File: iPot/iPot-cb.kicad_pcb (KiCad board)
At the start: 2 copper layers, 100 x 100 mm, 66 parts, among them CON1 12VDC, IC1 ATMEGA644-P, IC2 L298, P1 MOT2, P10 I2C3, P11 I2C4, P12 UART, P13 USB_PWR2, P14 ANALOG_IN, P15 PWM_IO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

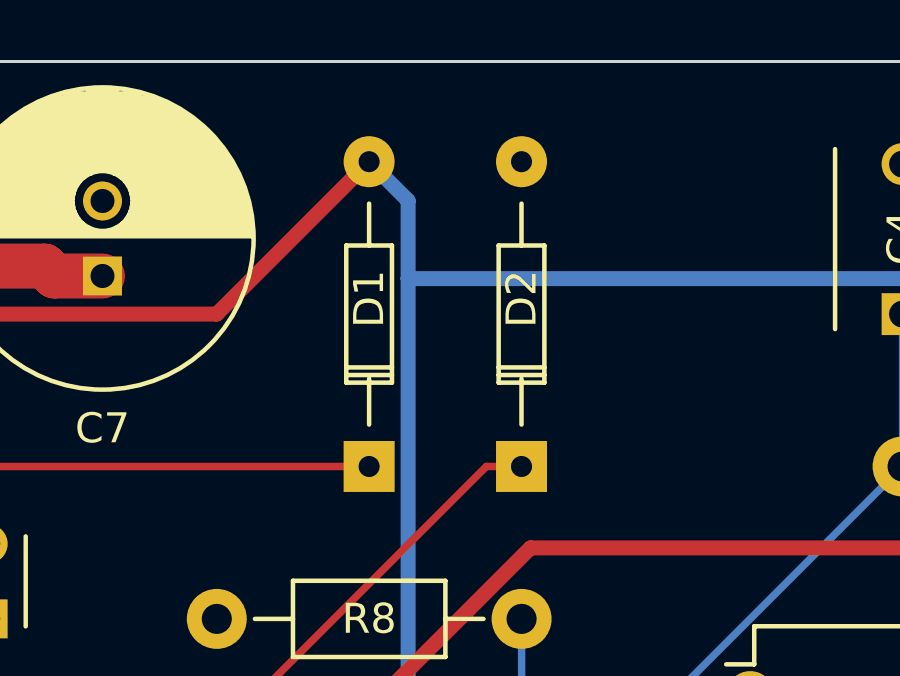
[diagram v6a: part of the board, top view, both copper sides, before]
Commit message: Fix diode footprint
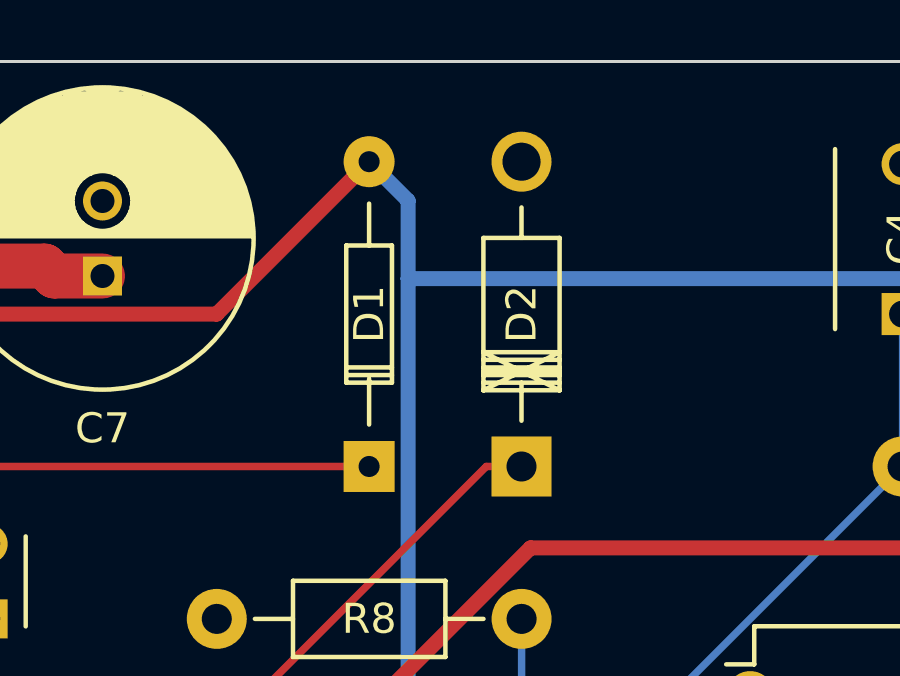
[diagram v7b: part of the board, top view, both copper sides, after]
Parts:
- D2: footprint Diodes_ThroughHole:Diode_DO-35_SOD27_Horizontal_RM10 -> Diodes_ThroughHole:Diode_DO-41_SOD81_Horizontal_RM10
- R7: value 270 -> 390
- R8: value 1k -> 680
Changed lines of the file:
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@@
     (links 170)
     (no_connects 1)
-    (area 49.511474 49.949999 152.490046 150.380714)
+    (area 49.949999 49.949999 150.050001 150.050001)
     (thickness 1.6)
     (drawings 5)
@@
     (descr "Diode, DO-35,  SOD27, Horizontal, RM 10mm")
     (tags "Diode, DO-35, SOD27, Horizontal, RM 10mm, 1N4148,")
-    (fp_text reference D1 (at 5.588 0 90) (layer F.SilkS)
+    (fp_text reference D1 (at 5.08 0 90) (layer F.SilkS)
       (effects (font (size 1 1) (thickness 0.15)))
     )
@@
     (pad 1 thru_hole rect (at 0.00052 -0.00254 270) (size 1.69926 1.69926) (drill 0.70104) (layers *.Cu *.Mask F.SilkS)
       (net 3 "Net-(C2-Pad1)"))
-    (model Diodes_ThroughHole.3dshapes/Diode_DO-35_SOD27_Horizontal_RM10.wrl
-      (at (xyz 0.2 0 0))
-      (scale (xyz 0.4 0.4 0.4))
-      (rotate (xyz 0 0 180))
-    )
-  )
-  (module Diodes_ThroughHole:Diode_DO-35_SOD27_Horizontal_RM10 locked (layer F.Cu)
-    (at 109.22 63.5 90)
-    (descr "Diode, DO-35,  SOD27, Horizontal, RM 10mm")
-    (tags "Diode, DO-35, SOD27, Horizontal, RM 10mm, 1N4148,")
-    (fp_text reference D2 (at 5.588 0 90) (layer F.SilkS)
-      (effects (font (size 1 1) (thickness 0.15)))
-    )
-    (fp_text value 1N5818 (at 4.41452 -3.55854 90) (layer F.Fab)
-      (effects (font (size 1 1) (thickness 0.15)))
-    )
-    (fp_line (start 7.36652 -0.00254) (end 8.76352 -0.00254) (layer F.SilkS) (width 0.15))
-    (fp_line (start 2.92152 -0.00254) (end 1.39752 -0.00254) (layer F.SilkS) (width 0.15))
-    (fp_line (start 3.30252 -0.76454) (end 3.30252 0.75946) (layer F.SilkS) (width 0.15))
-    (fp_line (start 3.04852 -0.76454) (end 3.04852 0.75946) (layer F.SilkS) (width 0.15))
-    (fp_line (start 2.79452 -0.00254) (end 2.79452 0.75946) (layer F.SilkS) (width 0.15))
-    (fp_line (start 2.79452 0.75946) (end 7.36652 0.75946) (layer F.SilkS) (width 0.15))
-    (fp_line (start 7.36652 0.75946) (end 7.36652 -0.76454) (layer F.SilkS) (width 0.15))
-    (fp_line (start 7.36652 -0.76454) (end 2.79452 -0.76454) (layer F.SilkS) (width 0.15))
-    (fp_line (start 2.79452 -0.76454) (end 2.79452 -0.00254) (layer F.SilkS) (width 0.15))
-    (pad 2 thru_hole circle (at 10.16052 -0.00254 270) (size 1.69926 1.69926) (drill 0.70104) (layers *.Cu *.Mask F.SilkS)
-      (net 2 GND))
-    (pad 1 thru_hole rect (at 0.00052 -0.00254 270) (size 1.69926 1.69926) (drill 0.70104) (layers *.Cu *.Mask F.SilkS)
-      (net 4 "Net-(C2-Pad2)"))
     (model Diodes_ThroughHole.3dshapes/Diode_DO-35_SOD27_Horizontal_RM10.wrl
       (at (xyz 0.2 0 0))
@@
       (effects (font (size 1 1) (thickness 0.15)))
     )
-    (fp_text value 270 (at 5.08 3.81) (layer F.Fab)
+    (fp_text value 390 (at 5.08 3.81) (layer F.Fab)
       (effects (font (size 1 1) (thickness 0.15)))
     )
@@
       (effects (font (size 1 1) (thickness 0.15)))
     )
-    (fp_text value 1k (at 5.08 3.81 180) (layer F.Fab)
+    (fp_text value 680 (at 5.08 3.81 180) (layer F.Fab)
       (effects (font (size 1 1) (thickness 0.15)))
     )
@@
     (pad 1 thru_hole circle (at -8.75 -3 90) (size 4 4) (drill 2.5) (layers *.Cu *.Mask F.SilkS))
   )
+  (module Diodes_ThroughHole:Diode_DO-41_SOD81_Horizontal_RM10 (layer F.Cu)
+    (at 109.22 63.5 90)
+    (descr "Diode, DO-41, SOD81, Horizontal, RM 10mm,")
+    (tags "Diode, DO-41, SOD81, Horizontal, RM 10mm, 1N4007, SB140,")
+    (fp_text reference D2 (at 5.08 0 90) (layer F.SilkS)
+      (effects (font (size 1 1) (thickness 0.15)))
+    )
+    (fp_text value 1N5818 (at 4.37134 -3.55854 90) (layer F.Fab)
+      (effects (font (size 1 1) (thickness 0.15)))
+    )
+    (fp_line (start 7.62 -0.00254) (end 8.636 -0.00254) (layer F.SilkS) (width 0.15))
+    (fp_line (start 2.794 -0.00254) (end 1.524 -0.00254) (layer F.SilkS) (width 0.15))
+    (fp_line (start 3.048 -1.27254) (end 3.048 1.26746) (layer F.SilkS) (width 0.15))
+    (fp_line (start 3.302 -1.27254) (end 3.302 1.26746) (layer F.SilkS) (width 0.15))
+    (fp_line (start 3.556 -1.27254) (end 3.556 1.26746) (layer F.SilkS) (width 0.15))
+    (fp_line (start 2.794 -1.27254) (end 2.794 1.26746) (layer F.SilkS) (width 0.15))
+    (fp_line (start 3.81 -1.27254) (end 2.54 1.26746) (layer F.SilkS) (width 0.15))
+    (fp_line (start 2.54 -1.27254) (end 3.81 1.26746) (layer F.SilkS) (width 0.15))
+    (fp_line (start 3.81 -1.27254) (end 3.81 1.26746) (layer F.SilkS) (width 0.15))
+    (fp_line (start 3.175 -1.27254) (end 3.175 1.26746) (layer F.SilkS) (width 0.15))
+    (fp_line (start 2.54 1.26746) (end 2.54 -1.27254) (layer F.SilkS) (width 0.15))
+    (fp_line (start 2.54 -1.27254) (end 7.62 -1.27254) (layer F.SilkS) (width 0.15))
+    (fp_line (start 7.62 -1.27254) (end 7.62 1.26746) (layer F.SilkS) (width 0.15))
+    (fp_line (start 7.62 1.26746) (end 2.54 1.26746) (layer F.SilkS) (width 0.15))
+    (pad 2 thru_hole circle (at 10.16 -0.00254 270) (size 1.99898 1.99898) (drill 1.27) (layers *.Cu *.Mask F.SilkS)
+      (net 2 GND))
+    (pad 1 thru_hole rect (at 0 -0.00254 270) (size 1.99898 1.99898) (drill 1.00076) (layers *.Cu *.Mask F.SilkS)
+      (net 4 "Net-(C2-Pad2)"))
+  )
   (gr_text "iPot control board v1.1.\nreleased under CERN OHL v1.2 or later." (at 124.46 96.52 90) (layer B.SilkS)
